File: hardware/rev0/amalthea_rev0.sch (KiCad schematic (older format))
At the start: 34 parts, among them J1 USB_B_Micro, J2 USB_B_Micro, J3 USB_A, J4 USB_B_Micro, J7 Conn_02x02_Counter_Clockwise, J8 Conn_Coaxial, J9 Conn_Coaxial, SW1 BTN_RECOVERY, SW2 BTN_DFU, SW3 BTN_RESET, U1 AP22814-SOT, U12 AP22814-SOT, Y1 DSC60xx

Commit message: Remove target PHY
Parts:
- removed J3: USB_A, amalthea:CONN-Amphenol-UE27AC54100, symbol Connector:USB_A
- removed J4: USB_B_Micro, Connector_USB:USB_Micro-B_Amphenol_10103594-0001LF_Horizontal, symbol Connector:USB_B_Micro
- removed R3: 10K, Capacitor_SMD:C_0402_1005Metric, symbol Device:R
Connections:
- net labels removed: TARGET_D+, TARGET_D-, TARGET_ID, TARGET_PHY_1V8, TARGET_VBUS_IN
- wire segments 183 -> 151
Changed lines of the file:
@@
 Wire Wire Line
 	1300 3700 1200 3700
-Wire Wire Line
-	9000 2900 9050 2900
-Connection ~ 9000 2900
-Wire Wire Line
-	9000 3000 9000 2900
-$Comp
-L power:GND #PWR08
-U 1 1 5DD6FDBE
-P 9000 3000
-F 0 "#PWR08" H 9000 2750 50  0001 C CNN
-F 1 "GND" H 9004 2828 50  0000 C CNN
-F 2 "" H 9000 3000 50  0001 C CNN
-F 3 "" H 9000 3000 50  0001 C CNN
-	1    9000 3000
-	1    0    0    -1
-$EndComp
-Wire Wire Line
-	9050 2900 9050 2850
-Wire Wire Line
-	8950 2900 9000 2900
-Wire Wire Line
-	8950 2850 8950 2900
-$Comp
-L Connector:USB_A J3
-U 1 1 5DD6DEF2
-P 8950 2450
-F 0 "J3" H 8721 2439 50  0000 R CNN
-F 1 "USB_A" H 8721 2349 50  0000 R CNN
-F 2 "amalthea:CONN-Amphenol-UE27AC54100" H 9100 2400 50  0001 C CNN
-F 3 " ~" H 9100 2400 50  0001 C CNN
-	1    8950 2450
-	-1   0    0    -1
-$EndComp
-Wire Wire Line
-	4000 3500 3600 3500
 $Sheet
 S 4000 3350 1700 1250
@@
 F0 "Target Section" 50
 F1 "target_side.sch" 50
-F2 "TARGET_ID" B R 5700 3950 50
-F3 "TARGET_D+" B R 5700 3750 50
-F4 "TARGET_D-" B R 5700 3850 50
-F5 "TARGET_VBUS" I R 5700 3550 50
-F6 "TARGET_PHY_1V8" O L 4000 3500 50
-F7 "TARGET_FAULT" I R 5700 4150 50
-F8 "A_PORT_POWER_ENABLE" O R 5700 4350 50
-F9 "ALLOW_POWER_VIA_TARGET_PORT" O R 5700 4450 50
 $EndSheet
-Wire Wire Line
-	9050 4200 9000 4200
-Connection ~ 9050 4200
-Wire Wire Line
-	9050 4250 9050 4200
-$Comp
-L power:GND #PWR09
-U 1 1 5DD6B00F
-P 9050 4250
-F 0 "#PWR09" H 9050 4000 50  0001 C CNN
-F 1 "GND" H 9054 4078 50  0000 C CNN
-F 2 "" H 9050 4250 50  0001 C CNN
-F 3 "" H 9050 4250 50  0001 C CNN
-	1    9050 4250
-	-1   0    0    -1
-$EndComp
-Wire Wire Line
-	9000 4200 9000 4150
-Wire Wire Line
-	9100 4200 9050 4200
-Wire Wire Line
-	9100 4150 9100 4200
-$Comp
-L Connector:USB_B_Micro J4
-U 1 1 5DD6B002
-P 9000 3750
-F 0 "J4" H 9056 4215 50  0000 C CNN
-F 1 "USB_B_Micro" H 9056 4125 50  0000 C CNN
-F 2 "Connector_USB:USB_Micro-B_Amphenol_10103594-0001LF_Horizontal" H 9150 3700 50  0001 C CNN
-F 3 "~" H 9150 3700 50  0001 C CNN
-	1    9000 3750
-	-1   0    0    -1
-$EndComp
 Wire Wire Line
 	8550 1600 8700 1600
@@
 64Mib HyperRAM
 Wire Wire Line
-	5700 3550 6200 3550
-Wire Wire Line
-	5700 3750 6300 3750
-Wire Wire Line
-	5700 3850 6400 3850
-Wire Wire Line
 	10700 2050 8450 2050
 Wire Wire Line
@@
 Wire Wire Line
 	8450 2250 8650 2250
-Wire Wire Line
-	6200 1500 6200 3550
-Connection ~ 6200 3550
-Wire Wire Line
-	6200 3550 8700 3550
-Wire Wire Line
-	6300 2450 6300 3750
-Wire Wire Line
-	6300 2450 8650 2450
-Connection ~ 6300 3750
-Wire Wire Line
-	6300 3750 8700 3750
-Wire Wire Line
-	6400 3850 6400 2550
-Wire Wire Line
-	6400 2550 8650 2550
-Connection ~ 6400 3850
-Wire Wire Line
-	6400 3850 8700 3850
 $Comp
 L Device:R R2
@@
 Wire Wire Line
 	3500 5300 4000 5300
-Wire Wire Line
-	4000 5200 3600 5200
-Wire Wire Line
-	3600 5200 3600 3500
 Text Label 5850 6750 0    50   ~ 0
 SIDEBAND_D+
@@
 Wire Wire Line
 	1700 2600 2150 2600
-Text Label 5950 4450 0    50   ~ 0
-VBUS_PASSTHROUGH_EN
-Text Label 5950 4350 0    50   ~ 0
-PROVIDE_A_PORT_VBUS
-Text Label 7200 2450 0    50   ~ 0
-TARGET_D+
-Text Label 7200 2550 0    50   ~ 0
-TARGET_D-
-Text Label 7200 3750 0    50   ~ 0
-TARGET_D+
-Text Label 7200 3850 0    50   ~ 0
-TARGET_D-
-Text Label 7200 3950 0    50   ~ 0
-TARGET_ID
-Text Label 7200 3550 0    50   ~ 0
-TARGET_VBUS_IN
 Text Label 8750 2050 0    50   ~ 0
 TARGET_VBUS_OUT
@@
 Text Label 3000 4800 0    50   ~ 0
 HOST_PHY_1V8
-Text Label 3600 4150 1    50   ~ 0
-TARGET_PHY_1V8
 $Comp
 L Switch:SW_SPST SW3
@@
 	1300 3050 1300 2950
 Wire Wire Line
-	8700 3950 5700 3950
-Wire Wire Line
 	5700 6200 5850 6200
 Wire Wire Line
@@
 	0    1    1    0
 $EndComp
-Wire Wire Line
-	5700 4150 5800 4150
-Text Label 5950 4150 0    50   ~ 0
-TARGET_FAULT
 Text Label 9050 6100 0    50   ~ 0
 DEBUG_SPI_MOSI
@@
 Wire Notes Line
 	3900 3200 500  3200
-Wire Wire Line
-	5950 4350 5700 4350
-Wire Wire Line
-	5950 4450 5700 4450
 $Comp
 L support_hardware:AP22804-SOT U12
@@
 	9650 1350 10000 1350
 $Comp
-L Device:R R3
-U 1 1 5DEBAF7B
-P 6800 4050
-F 0 "R3" V 6900 4050 50  0000 C CNN
-F 1 "10K" V 6800 4050 50  0000 C CNN
-F 2 "Capacitor_SMD:C_0402_1005Metric" V 6730 4050 50  0001 C CNN
-F 3 "~" H 6800 4050 50  0001 C CNN
-	1    6800 4050
-	0    1    1    0
-$EndComp
-Wire Wire Line
-	5800 4150 5800 4050
-Wire Wire Line
-	5800 4050 6650 4050
-Connection ~ 5800 4150
-Wire Wire Line
-	5800 4150 5950 4150
-$Comp
-L power:+3V3 #PWR0117
-U 1 1 5DEC924F
-P 7000 4050
-F 0 "#PWR0117" H 7000 3900 50  0001 C CNN
-F 1 "+3V3" V 7014 4178 50  0000 L CNN
-F 2 "" H 7000 4050 50  0001 C CNN
-F 3 "" H 7000 4050 50  0001 C CNN
-	1    7000 4050
-	0    1    1    0
-$EndComp
-Wire Wire Line
-	7000 4050 6950 4050
-$Comp
 L Device:C C53

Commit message: Rough out LVDS
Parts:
- removed C53: 10uF, Capacitor_SMD:C_0805_2012Metric, symbol Device:C
- removed C54, C55: 0.1uF, Capacitor_SMD:C_0402_1005Metric, symbol Device:C
- removed R1, R2: 10K, Resistor_SMD:R_0402_1005Metric, symbol Device:R
- removed U1, U12: AP22814-SOT, gsg-modules:SOT25, symbol support_hardware:AP22804-SOT
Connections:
- net labels removed: PROVIDE_A_PORT_VBUS, TARGET_FAULT, TARGET_VBUS_OUT, VBUS_PASSTHROUGH_EN
- wire segments 151 -> 119
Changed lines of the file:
@@
 F1 "target_side.sch" 50
 $EndSheet
-Wire Wire Line
-	8550 1600 8700 1600
-Text Label 10000 1350 0    50   ~ 0
-TARGET_FAULT
-Text Label 8100 1200 2    50   ~ 0
-PROVIDE_A_PORT_VBUS
-Text Label 8100 1850 2    50   ~ 0
-VBUS_PASSTHROUGH_EN
 $Sheet
 S 4000 1900 1700 950
@@
 64Mib HyperRAM
 Wire Wire Line
-	10700 2050 8450 2050
-Wire Wire Line
-	8450 2050 8450 2250
-Wire Wire Line
-	8450 2250 8650 2250
-$Comp
-L Device:R R2
-U 1 1 5DFA3A73
-P 7950 1700
-F 0 "R2" V 8050 1700 50  0000 C CNN
-F 1 "10K" V 7950 1700 50  0000 C CNN
-F 2 "Resistor_SMD:R_0402_1005Metric" V 7880 1700 50  0001 C CNN
-F 3 "~" H 7950 1700 50  0001 C CNN
-	1    7950 1700
-	0    1    -1   0
-$EndComp
-Wire Wire Line
 	3200 6900 3200 6000
 Wire Wire Line
@@
 Wire Wire Line
 	1700 2600 2150 2600
-Text Label 8750 2050 0    50   ~ 0
-TARGET_VBUS_OUT
 Text Label 1300 3900 0    50   ~ 0
 HOST_D+
@@
 	3900 3200 500  3200
 $Comp
-L support_hardware:AP22804-SOT U12
-U 1 1 5DDCF875
-P 8800 1450
-F 0 "U12" H 9050 1622 50  0000 C CNN
-F 1 "AP22814-SOT" H 9050 1532 50  0000 C CNN
-F 2 "gsg-modules:SOT25" H 8800 1450 50  0001 C CNN
-F 3 "" H 8800 1450 50  0001 C CNN
-	1    8800 1450
-	1    0    0    -1
-$EndComp
-$Comp
-L power:GND #PWR0114
-U 1 1 5DDE27E4
-P 8550 1600
-F 0 "#PWR0114" H 8550 1350 50  0001 C CNN
-F 1 "GND" V 8554 1472 50  0000 R CNN
-F 2 "" H 8550 1600 50  0001 C CNN
-F 3 "" H 8550 1600 50  0001 C CNN
-	1    8550 1600
-	0    1    1    0
-$EndComp
-Wire Wire Line
-	9400 1600 10700 1600
-Wire Wire Line
-	10700 1600 10700 2050
-Wire Wire Line
-	8700 1700 8250 1700
-Connection ~ 8250 1700
-Wire Wire Line
-	8250 1700 8100 1700
-Wire Wire Line
-	8250 1850 8100 1850
-Wire Wire Line
-	8250 1700 8250 1850
-Wire Wire Line
-	7800 1700 7650 1700
-Wire Wire Line
-	7650 1700 7650 1500
-Connection ~ 7650 1500
-Wire Wire Line
-	7650 1500 8700 1500
-$Comp
-L Device:R R1
-U 1 1 5DFB954D
-P 7950 1050
-F 0 "R1" V 7900 850 50  0000 C CNN
-F 1 "10K" V 7950 1050 50  0000 C CNN
-F 2 "Resistor_SMD:R_0402_1005Metric" V 7880 1050 50  0001 C CNN
-F 3 "~" H 7950 1050 50  0001 C CNN
-	1    7950 1050
-	0    -1   1    0
-$EndComp
-Wire Wire Line
-	6200 1500 6650 1500
-$Comp
-L support_hardware:AP22804-SOT U1
-U 1 1 5DE0E59A
-P 8800 800
-F 0 "U1" H 9050 972 50  0000 C CNN
-F 1 "AP22814-SOT" H 9050 882 50  0000 C CNN
-F 2 "gsg-modules:SOT25" H 8800 800 50  0001 C CNN
-F 3 "" H 8800 800 50  0001 C CNN
-	1    8800 800
-	1    0    0    -1
-$EndComp
-$Comp
-L power:+5V #PWR0115
-U 1 1 5DE172C2
-P 8350 850
-F 0 "#PWR0115" H 8350 700 50  0001 C CNN
-F 1 "+5V" H 8364 1023 50  0000 C CNN
-F 2 "" H 8350 850 50  0001 C CNN
-F 3 "" H 8350 850 50  0001 C CNN
-	1    8350 850
-	1    0    0    -1
-$EndComp
-$Comp
-L power:GND #PWR0116
-U 1 1 5DE20196
-P 7800 950
-F 0 "#PWR0116" H 7800 700 50  0001 C CNN
-F 1 "GND" V 7804 822 50  0000 R CNN
-F 2 "" H 7800 950 50  0001 C CNN
-F 3 "" H 7800 950 50  0001 C CNN
-	1    7800 950
-	0    1    1    0
-$EndComp
-Wire Wire Line
-	8100 1050 8250 1050
-Wire Wire Line
-	9400 950  10700 950
-Wire Wire Line
-	10700 950  10700 1600
-Connection ~ 10700 1600
-Wire Wire Line
-	8250 1050 8250 1200
-Wire Wire Line
-	8250 1200 8100 1200
-Connection ~ 8250 1050
-Wire Wire Line
-	8250 1050 8700 1050
-Wire Wire Line
-	8350 850  8700 850
-Wire Wire Line
-	7800 950  7800 1050
-Wire Wire Line
-	7800 950  8700 950
-Connection ~ 7800 950
-Wire Wire Line
-	9650 1050 9650 1350
-Wire Wire Line
-	9400 1050 9650 1050
-Wire Wire Line
-	9400 1700 9650 1700
-Wire Wire Line
-	9650 1700 9650 1350
-Connection ~ 9650 1350
-Wire Wire Line
-	9650 1350 10000 1350
-$Comp
-L Device:C C53
-U 1 1 5DED4B80
-P 10850 950
-F 0 "C53" V 10600 950 50  0000 C CNN
-F 1 "10uF" V 10690 950 50  0000 C CNN
-F 2 "Capacitor_SMD:C_0805_2012Metric" H 10888 800 50  0001 C CNN
-F 3 "~" H 10850 950 50  0001 C CNN
-	1    10850 950
-	0    1    1    0
-$EndComp
-Connection ~ 10700 950
-$Comp
-L power:GND #PWR0118
-U 1 1 5DED5921
-P 11000 950
-F 0 "#PWR0118" H 11000 700 50  0001 C CNN
-F 1 "GND" H 11100 800 50  0000 R CNN
-F 2 "" H 11000 950 50  0001 C CNN
-F 3 "" H 11000 950 50  0001 C CNN
-	1    11000 950
-	0    -1   -1   0
-$EndComp
-$Comp
-L Device:C C54
-U 1 1 5DF2ADB4
-P 6650 950
-F 0 "C54" H 6765 995 50  0000 L CNN
-F 1 "0.1uF" H 6765 905 50  0000 L CNN
-F 2 "Capacitor_SMD:C_0402_1005Metric" H 6688 800 50  0001 C CNN
-F 3 "~" H 6650 950 50  0001 C CNN
-	1    6650 950
-	1    0    0    -1
-$EndComp
-$Comp
-L power:GND #PWR0119
-U 1 1 5DF2CA53
-P 6650 1200
-F 0 "#PWR0119" H 6650 950 50  0001 C CNN
-F 1 "GND" H 6654 1028 50  0000 C CNN
-F 2 "" H 6650 1200 50  0001 C CNN
-F 3 "" H 6650 1200 50  0001 C CNN
-	1    6650 1200
-	1    0    0    -1
-$EndComp
-Wire Wire Line
-	6650 1200 6650 1100
-$Comp
-L power:+5V #PWR0120
-U 1 1 5DF36D7D
-P 6650 700
-F 0 "#PWR0120" H 6650 550 50  0001 C CNN
-F 1 "+5V" H 6664 873 50  0000 C CNN
-F 2 "" H 6650 700 50  0001 C CNN
-F 3 "" H 6650 700 50  0001 C CNN
-	1    6650 700
-	1    0    0    -1
-$EndComp
-Wire Wire Line
-	6650 700  6650 800
-$Comp
-L Device:C C55
-U 1 1 5DF41314
-P 6650 1650
-F 0 "C55" H 6765 1695 50  0000 L CNN
-F 1 "0.1uF" H 6765 1605 50  0000 L CNN
-F 2 "Capacitor_SMD:C_0402_1005Metric" H 6688 1500 50  0001 C CNN
-F 3 "~" H 6650 1650 50  0001 C CNN
-	1    6650 1650
-	1    0    0    -1
-$EndComp
-Connection ~ 6650 1500
-Wire Wire Line
-	6650 1500 7650 1500
-$Comp
-L power:GND #PWR0121
-U 1 1 5DF42827
-P 6650 1900
-F 0 "#PWR0121" H 6650 1650 50  0001 C CNN
-F 1 "GND" H 6654 1728 50  0000 C CNN
-F 2 "" H 6650 1900 50  0001 C CNN
-F 3 "" H 6650 1900 50  0001 C CNN
-	1    6650 1900
-	1    0    0    -1
-$EndComp
-Wire Wire Line
-	6650 1900 6650 1800
-$Comp
 L Device:LED D?

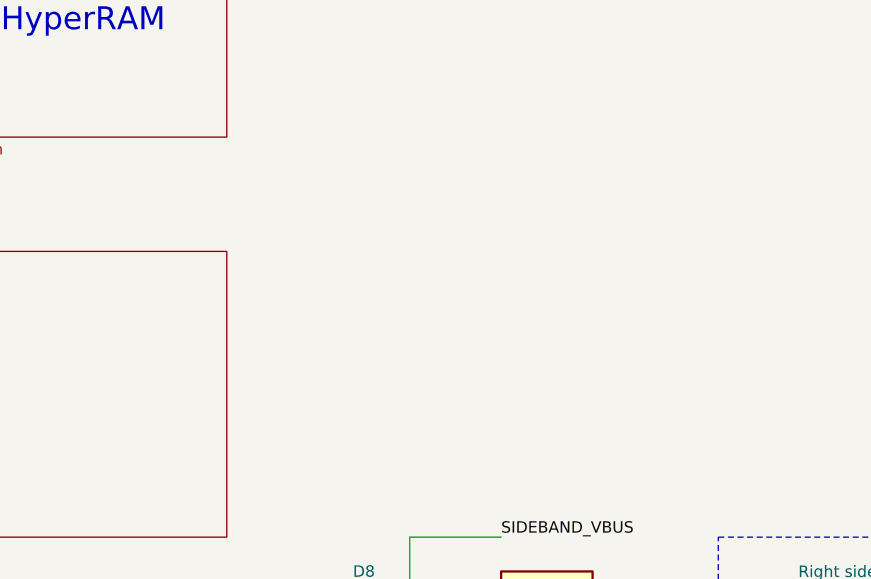
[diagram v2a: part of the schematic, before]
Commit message: Add baluns, matching, TXCO, decoupling
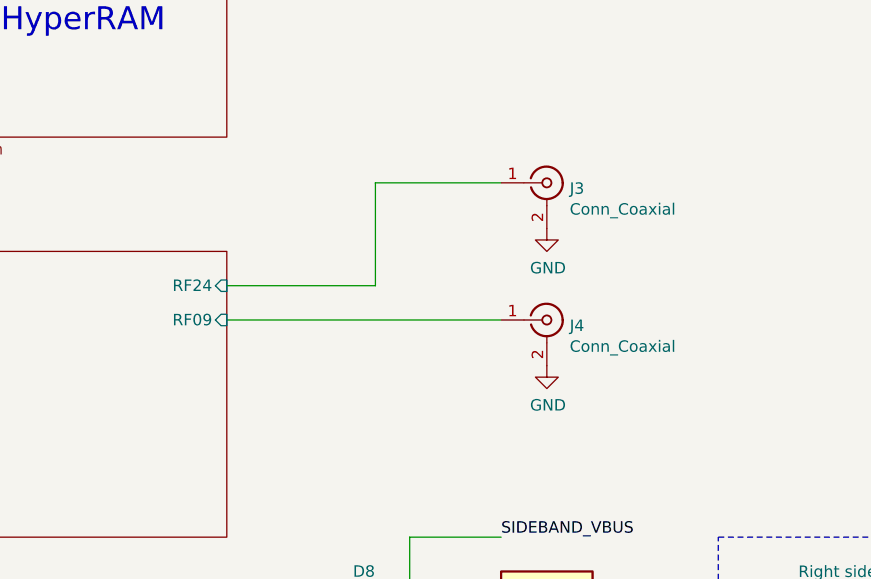
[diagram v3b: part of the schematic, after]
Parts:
- added J3, J4: Conn_Coaxial, symbol Connector:Conn_Coaxial
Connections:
- net GND: now also J3.2 (Ext), J4.2 (Ext)
- new net Target Section/RF09: J4.1 (In)
- new net Target Section/RF24: J3.1 (In)
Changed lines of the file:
@@
 F0 "Target Section" 50
 F1 "target_side.sch" 50
+F2 "RF24" I R 5700 3500 50
+F3 "RF09" I R 5700 3650 50
 $EndSheet
 $Sheet
@@
 Wire Wire Line
 	5850 6050 5700 6050
+$Comp
+L Connector:Conn_Coaxial J3
+U 1 1 5E946A30
+P 7100 3050
+F 0 "J3" H 7200 3025 50  0000 L CNN
+F 1 "Conn_Coaxial" H 7200 2934 50  0000 L CNN
+F 2 "" H 7100 3050 50  0001 C CNN
+F 3 " ~" H 7100 3050 50  0001 C CNN
+	1    7100 3050
+	1    0    0    -1
+$EndComp
+$Comp
+L Connector:Conn_Coaxial J4
+U 1 1 5E94862D
+P 7100 3650
+F 0 "J4" H 7200 3625 50  0000 L CNN
+F 1 "Conn_Coaxial" H 7200 3534 50  0000 L CNN
+F 2 "" H 7100 3650 50  0001 C CNN
+F 3 " ~" H 7100 3650 50  0001 C CNN
+	1    7100 3650
+	1    0    0    -1
+$EndComp
+Wire Wire Line
+	5700 3650 6900 3650
+Wire Wire Line
+	5700 3500 6350 3500
+Wire Wire Line
+	6350 3500 6350 3050
+Wire Wire Line
+	6350 3050 6900 3050
+$Comp
+L power:GND #PWR0114
+U 1 1 5E952A4F
+P 7100 3250
+F 0 "#PWR0114" H 7100 3000 50  0001 C CNN
+F 1 "GND" H 7105 3077 50  0000 C CNN
+F 2 "" H 7100 3250 50  0001 C CNN
+F 3 "" H 7100 3250 50  0001 C CNN
+	1    7100 3250
+	1    0    0    -1
+$EndComp
+$Comp
+L power:GND #PWR0115
+U 1 1 5E952D40
+P 7100 3850
+F 0 "#PWR0115" H 7100 3600 50  0001 C CNN
+F 1 "GND" H 7105 3677 50  0000 C CNN
+F 2 "" H 7100 3850 50  0001 C CNN
+F 3 "" H 7100 3850 50  0001 C CNN
+	1    7100 3850
+	1    0    0    -1
+$EndComp
 $EndSCHEMATC

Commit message: Do a bunch of placement
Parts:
- J3, J4: footprint (none) -> amalthea:SMA-EDGE
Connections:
- net Target Section/RF09: now also J3.1 (In); no longer J4.1 (In)
- net Target Section/RF24: now also J4.1 (In); no longer J3.1 (In)
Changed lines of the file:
@@
 F0 "Target Section" 50
 F1 "target_side.sch" 50
-F2 "RF24" I R 5700 3500 50
-F3 "RF09" I R 5700 3650 50
+F2 "RF24" I R 5700 3650 50
+F3 "RF09" I R 5700 3500 50
 $EndSheet
 $Sheet
@@
 F 0 "J3" H 7200 3025 50  0000 L CNN
 F 1 "Conn_Coaxial" H 7200 2934 50  0000 L CNN
-F 2 "" H 7100 3050 50  0001 C CNN
+F 2 "amalthea:SMA-EDGE" H 7100 3050 50  0001 C CNN
 F 3 " ~" H 7100 3050 50  0001 C CNN
 	1    7100 3050
@@
 F 0 "J4" H 7200 3625 50  0000 L CNN
 F 1 "Conn_Coaxial" H 7200 3534 50  0000 L CNN
-F 2 "" H 7100 3650 50  0001 C CNN
+F 2 "amalthea:SMA-EDGE" H 7100 3650 50  0001 C CNN
 F 3 " ~" H 7100 3650 50  0001 C CNN
 	1    7100 3650
